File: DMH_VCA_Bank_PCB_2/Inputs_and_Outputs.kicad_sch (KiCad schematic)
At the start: 24 parts, among them J0 Conn_01x01, J1 TS_Jack_6.35mm_Sw, J10 TS_Jack_6.35mm_Sw, J2 TS_Jack_6.35mm_Sw, J200 IDC_02x05, J3 TS_Jack_6.35mm_Sw, J4 TS_Jack_6.35mm_Sw, J5 TS_Jack_6.35mm_Sw, J50 Conn_01x08, J6 TS_Jack_6.35mm_Sw, J60 Conn_01x08, J7 TS_Jack_6.35mm_Sw, J70 Conn_01x08, J8 TS_Jack_6.35mm_Sw, J9 TS_Jack_6.35mm_Sw

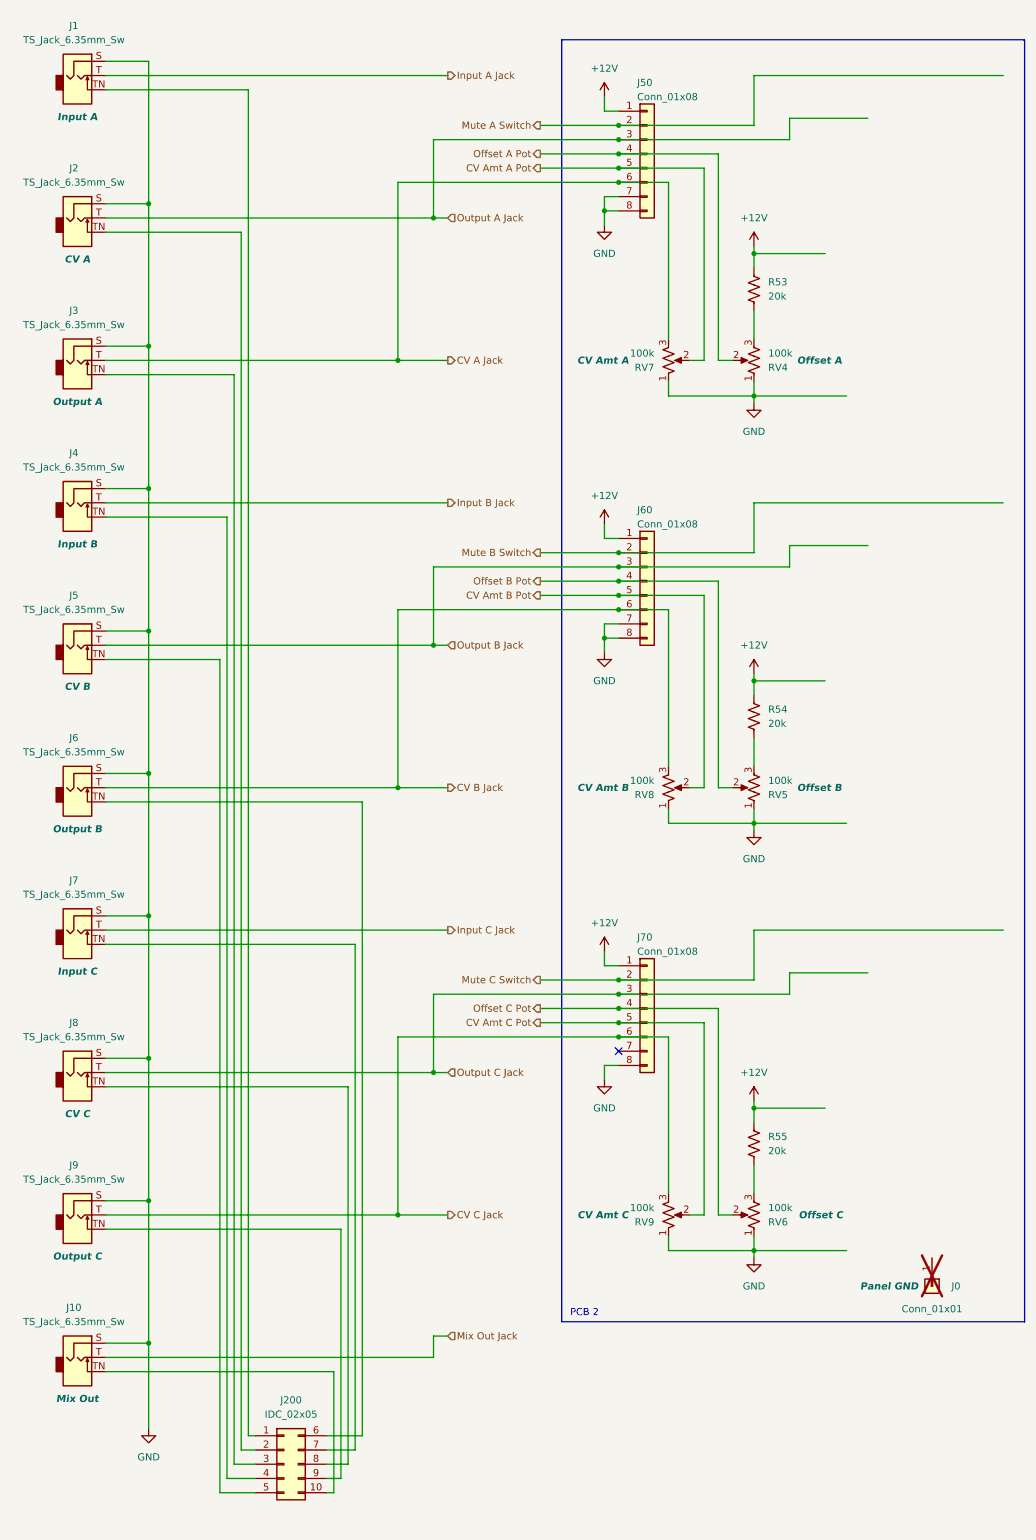
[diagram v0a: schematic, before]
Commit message: Finished schematic of PCB 2
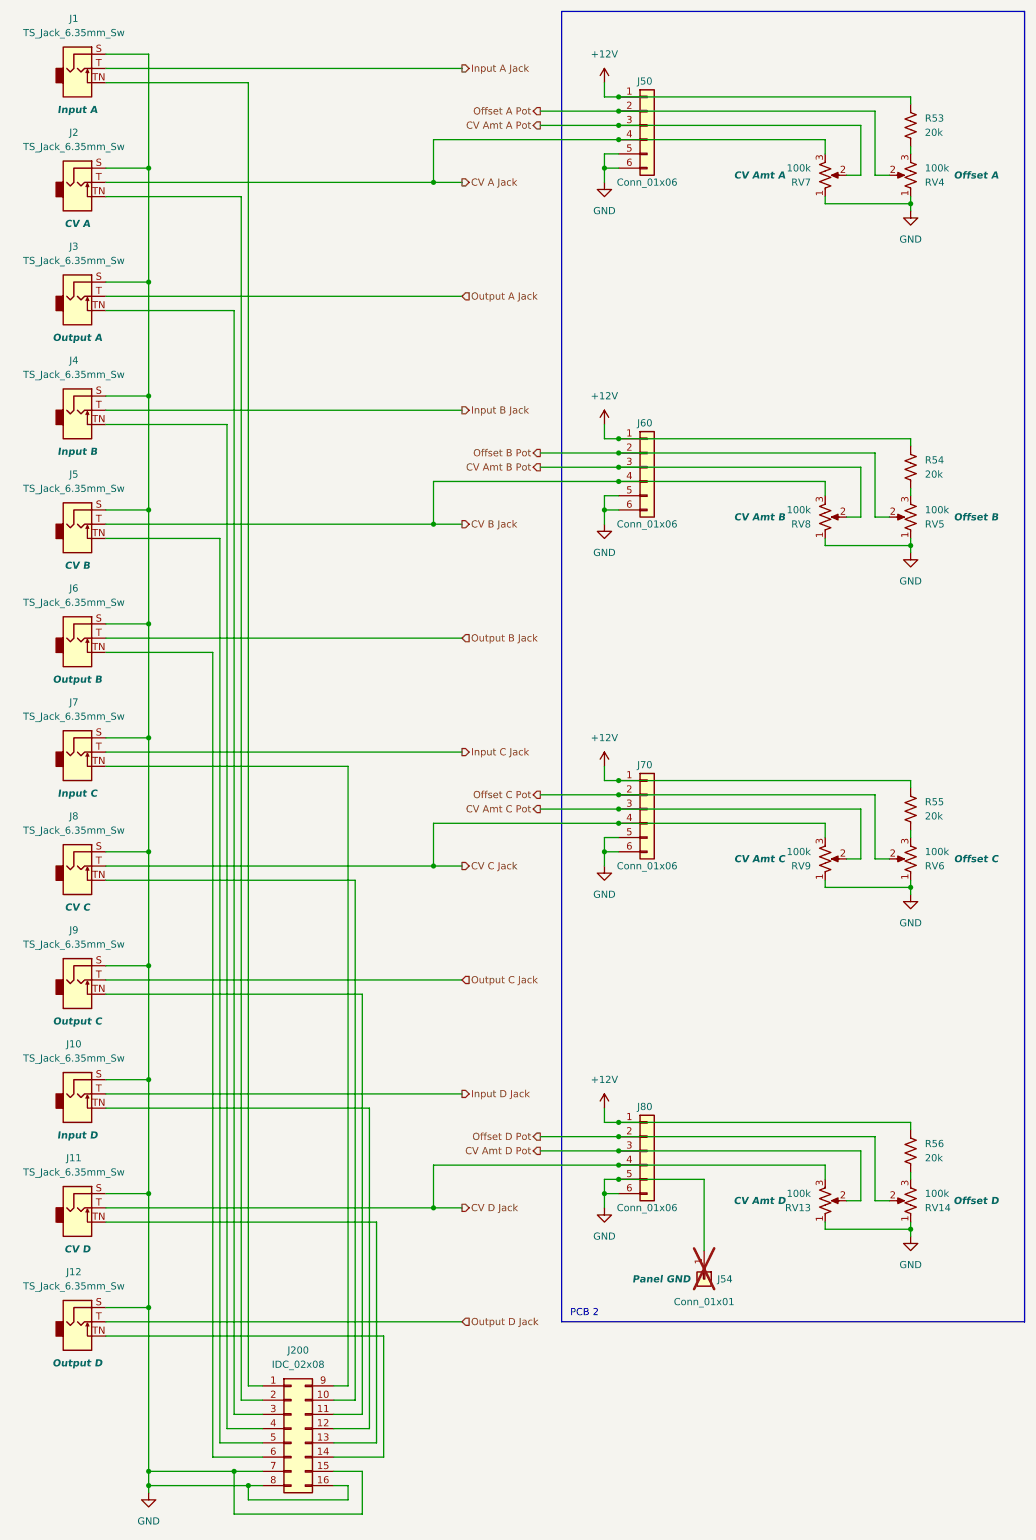
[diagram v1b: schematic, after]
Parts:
- removed J60, J70: Conn_01x08, Connector_PinHeader_2.54mm:PinHeader_1x08_P2.54mm_Vertical, symbol Connector_Generic:Conn_01x08
- added J11, J12: TS_Jack_6.35mm_Sw, SynthStuff:CUI_MJ-63052A, symbol SynthStuff:TS_Jack_6.35mm_Sw
- added J60, J70, J80: Conn_01x06, Connector_PinSocket_2.54mm:PinSocket_1x08_P2.54mm_Vertical, symbol Connector_Generic:Conn_01x06
- added R56: 20k, Resistor_THT:R_Axial_DIN0207_L6.3mm_D2.5mm_P7.62mm_Horizontal, symbol Device:R_US
- added RV13: 100k, SynthStuff:Potentiometer_TT_P110KH1, symbol Device:R_Potentiometer_US
- added RV14: 100k, SynthStuff:Potentiometer_Alpha_RD901F-40-00D_Single_Vertical, symbol Device:R_Potentiometer_US
- J10: Function Mix Out -> Input D
- J200: value IDC_02x05 -> IDC_02x08; footprint SynthStuff:IDC-Header_2x05_P2.54mm_Vertical_BackBone -> SynthStuff:IDC-Header_2x08_P2.54mm_Vertical_BackBone; symbol SynthStuff:BackBone_Connector_10Pin -> SynthStuff:BackBone_Connector_16Pin
- J50: value Conn_01x08 -> Conn_01x06; footprint Connector_PinHeader_2.54mm:PinHeader_1x08_P2.54mm_Vertical -> Connector_PinSocket_2.54mm:PinSocket_1x08_P2.54mm_Vertical; symbol Connector_Generic:Conn_01x08 -> Connector_Generic:Conn_01x06
- renumbered J0 to J54
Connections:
- net Mute A Switch is gone; now on net Offset A Pot: J50.2 (Pin_2)
- net +12V: now also J60.1 (Pin_1), J70.1 (Pin_1), J80.1 (Pin_1), R56.2
- net CV A Jack: now also J2.T, J50.4 (Pin_4); no longer J3.T, J50.6 (Pin_6)
- net CV Amt A Pot: now also J50.3 (Pin_3); no longer J50.5 (Pin_5)
- net CV Amt B Pot: now also J60.3 (Pin_3)
- net CV Amt C Pot: now also J70.3 (Pin_3)
- net CV B Jack: now also J5.T, J60.4 (Pin_4); no longer J6.T
- net CV C Jack: now also J8.T, J70.4 (Pin_4); no longer J9.T
- net GND: now also J200.15 (Pin_15), J200.16 (Pin_16), J200.7 (Pin_7), J200.8 (Pin_8), J50.5 (Pin_5), J50.6 (Pin_6), J54.1 (Pin_1), J11.S, J12.S, J60.5 (Pin_5), J60.6 (Pin_6), J70.5 (Pin_5), J70.6 (Pin_6), J80.5 (Pin_5), J80.6 (Pin_6), RV13.1, RV14.1; no longer J50.7 (Pin_7), J50.8 (Pin_8)
- net Offset A Pot: no longer J50.4 (Pin_4)
- net Offset B Pot: now also J60.2 (Pin_2)
- net Offset C Pot: now also J70.2 (Pin_2)
- net Output A Jack: now also J3.T; no longer J2.T, J50.3 (Pin_3)
- net Output B Jack: now also J6.T; no longer J5.T
- net Output C Jack: now also J9.T; no longer J8.T
- net at J9.TN: now also J200.11 (Pin_11); no longer J200.9 (Pin_9)
- net at J200.10 (Pin_10): now also J8.TN; no longer J10.TN
- net at J7.TN: now also J200.9 (Pin_9); no longer J200.7 (Pin_7)
- net Mix Out Jack renamed Input D Jack
- new net: J10.TN, J200.12 (Pin_12)
- new net: J11.TN, J200.13 (Pin_13)
- new net: J12.TN, J200.14 (Pin_14)
- new net: R56.1, RV14.3
- new net CV Amt D Pot: J80.3 (Pin_3), RV13.2
- new net CV D Jack: J11.T, J80.4 (Pin_4), RV13.3
- new net Offset D Pot: J80.2 (Pin_2), RV14.2
- new net Output D Jack: J12.T
- no-connect marks 1 -> 0
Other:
- moved on the sheet: J1, J10, J2, J3, J4, J5, J54, J6, J7, J8, J9, R53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

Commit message: Finished PCB 2
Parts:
- J50, J60, J70, J80: footprint Connector_PinSocket_2.54mm:PinSocket_1x08_P2.54mm_Vertical -> Connector_PinSocket_2.54mm:PinSocket_1x06_P2.54mm_Vertical
- renumbered J54 to J0
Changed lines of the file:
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@@
 			)
 		)
-		(property "Footprint" "Connector_PinSocket_2.54mm:PinSocket_1x08_P2.54mm_Vertical"
+		(property "Footprint" "Connector_PinSocket_2.54mm:PinSocket_1x06_P2.54mm_Vertical"
 			(at 127 95.25 0)
 			(effects
@@
 			)
 		)
-		(property "Footprint" "Connector_PinSocket_2.54mm:PinSocket_1x08_P2.54mm_Vertical"
+		(property "Footprint" "Connector_PinSocket_2.54mm:PinSocket_1x06_P2.54mm_Vertical"
 			(at 127 34.29 0)
 			(effects
@@
 		(on_board yes)
 		(dnp yes)
-		(property "Reference" "J54"
+		(property "Reference" "J0"
 			(at 142.24 240.03 90)
 			(effects
@@
 			(project "DMH_VCA_Bank_PCB_2"
 				(path "/58f4306d-5387-4983-bb08-41a2313fd315/7b52706a-7501-4bd9-bd96-319206c66019"
-					(reference "J54")
+					(reference "J0")
 					(unit 1)
 				)
@@
 			)
 		)
-		(property "Footprint" "Connector_PinSocket_2.54mm:PinSocket_1x08_P2.54mm_Vertical"
+		(property "Footprint" "Connector_PinSocket_2.54mm:PinSocket_1x06_P2.54mm_Vertical"
 			(at 127 156.21 0)
 			(effects
@@
 			)
 		)
-		(property "Footprint" "Connector_PinSocket_2.54mm:PinSocket_1x08_P2.54mm_Vertical"
+		(property "Footprint" "Connector_PinSocket_2.54mm:PinSocket_1x06_P2.54mm_Vertical"
 			(at 127 217.17 0)
 			(effects
